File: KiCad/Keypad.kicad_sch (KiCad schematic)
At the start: 21 parts, among them J1 SPOX, J2 Molex, J3 USB-C, U1 ESP32-WROOM-32, U2 SP3458, U3 FT231XQ, U4 LMR16006YQ3

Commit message: Kicad tidy
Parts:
- C2: Note X7R or X5R 0603 -> (none)
- C3: Note 0603 or 0805 -> 0805
- C4: Note 0603 or 0805 -> 1206
- U1: footprint RevK:ESP32-WROOM-32 -> RF_Module:ESP32-WROOM-32
- U2: footprint Package_SO:SO-8_3.9x4.9mm_P1.27mm -> Package_SO:SO-8_5.3x6.2mm_P1.27mm
- U3: footprint RevK:QFN-20-1EP_4x4mm_P0.5mm_EP2.5x2.5mm -> Package_DFN_QFN:QFN-20-1EP_4x4mm_P0.5mm_EP2.5x2.5mm
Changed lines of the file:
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@@
   (title_block
     (title "Galaxy Keypad controller")
-    (date "2021-07-20")
+    (date "${DATE}")
     (rev "5")
     (company "Adrian Kennard Andrews & Arnold Ltd")
@@
     (property "Reference" "U2" (id 0) (at 106.68 152.019 0))
     (property "Value" "SP3458" (id 1) (at 106.68 154.3304 0))
-    (property "Footprint" "Package_SO:SO-8_3.9x4.9mm_P1.27mm" (id 2) (at 106.045 176.53 0)
+    (property "Footprint" "Package_SO:SO-8_5.3x6.2mm_P1.27mm" (id 2) (at 106.045 176.53 0)
       (effects (font (size 1.27 1.27)) hide)
     )
@@
     (property "Reference" "U3" (id 0) (at 172.085 88.7476 0))
     (property "Value" "FT231XQ" (id 1) (at 172.085 91.059 0))
-    (property "Footprint" "RevK:QFN-20-1EP_4x4mm_P0.5mm_EP2.5x2.5mm" (id 2) (at 206.375 136.525 0)
+    (property "Footprint" "Package_DFN_QFN:QFN-20-1EP_4x4mm_P0.5mm_EP2.5x2.5mm" (id 2) (at 206.375 136.525 0)
       (effects (font (size 1.27 1.27)) hide)
     )
@@
     (property "Reference" "U1" (id 0) (at 69.215 32.2326 0))
     (property "Value" "ESP32-WROOM-32" (id 1) (at 69.215 34.544 0))
-    (property "Footprint" "RevK:ESP32-WROOM-32" (id 2) (at 69.215 110.49 0)
+    (property "Footprint" "RF_Module:ESP32-WROOM-32" (id 2) (at 69.215 110.49 0)
       (effects (font (size 1.27 1.27)) hide)
     )
@@
     (pin "4")
   )
-  (symbol (lib_id "RevK:Hidden") (at 249.555 42.545 0) (unit 1)
-    (in_bom yes) (on_board yes)
-    (property "Reference" "C2" (id 0) (at 248.92 42.545 0)
+  (symbol (lib_name "Hidden_1") (lib_id "RevK:Hidden") (at 249.555 42.545 0) (unit 1)
+    (in_bom yes) (on_board yes)
+    (property "Reference" "C2" (id 0) (at 250.19 42.545 0)
       (effects (font (size 1.27 1.27)) (justify left))
     )
@@
       (effects (font (size 1.27 1.27)) hide)
     )
-    (property "Note" "X7R or X5R 0603" (id 4) (at 249.555 42.545 0)
+    (property "Note" "" (id 4) (at 249.555 42.545 0)
+      (effects (font (size 1.27 1.27)) hide)
+    )
+    (property "Part No" "" (id 5) (at 249.555 42.545 0)
       (effects (font (size 1.27 1.27)) hide)
     )
     (pin "~")
   )
-  (symbol (lib_id "RevK:Hidden") (at 249.555 44.45 0) (unit 1)
-    (in_bom yes) (on_board yes)
-    (property "Reference" "C3" (id 0) (at 248.92 44.45 0)
+  (symbol (lib_name "Hidden_2") (lib_id "RevK:Hidden") (at 249.555 44.45 0) (unit 1)
+    (in_bom yes) (on_board yes)
+    (property "Reference" "C3" (id 0) (at 250.19 44.45 0)
       (effects (font (size 1.27 1.27)) (justify left))
     )
@@
       (effects (font (size 1.27 1.27)) hide)
     )
-    (property "Note" "0603 or 0805" (id 4) (at 249.555 44.45 0)
+    (property "Note" "0805" (id 4) (at 249.555 44.45 0)
+      (effects (font (size 1.27 1.27)) hide)
+    )
+    (property "Part No" "" (id 5) (at 249.555 44.45 0)
       (effects (font (size 1.27 1.27)) hide)
     )
     (pin "~")
   )
-  (symbol (lib_id "RevK:Hidden") (at 249.555 46.355 0) (unit 1)
-    (in_bom yes) (on_board yes)
-    (property "Reference" "C4" (id 0) (at 248.92 46.355 0)
+  (symbol (lib_name "Hidden_3") (lib_id "RevK:Hidden") (at 249.555 46.355 0) (unit 1)
+    (in_bom yes) (on_board yes)
+    (property "Reference" "C4" (id 0) (at 250.19 46.355 0)
       (effects (font (size 1.27 1.27)) (justify left))
     )
@@
       (effects (font (size 1.27 1.27)) hide)
     )
-    (property "Note" "0603 or 0805" (id 4) (at 249.555 46.355 0)
+    (property "Note" "1206" (id 4) (at 249.555 46.355 0)
+      (effects (font (size 1.27 1.27)) hide)
+    )
+    (property "Part No" "" (id 5) (at 249.555 46.355 0)
       (effects (font (size 1.27 1.27)) hide)
     )
     (pin "~")
   )
-  (symbol (lib_id "RevK:Hidden") (at 249.555 48.26 0) (unit 1)
-    (in_bom yes) (on_board yes)
-    (property "Reference" "L1" (id 0) (at 248.92 48.26 0)
+  (symbol (lib_name "Hidden_4") (lib_id "RevK:Hidden") (at 249.555 48.26 0) (unit 1)
+    (in_bom yes) (on_board yes)
+    (property "Reference" "L1" (id 0) (at 250.19 48.26 0)
       (effects (font (size 1.27 1.27)) (justify left))
     )
@@
       (effects (font (size 1.27 1.27)) hide)
     )
+    (property "Note" "" (id 6) (at 256.54 58.42 0))
     (pin "~")
   )
   (symbol (lib_id "RevK:Hidden") (at 249.555 50.165 0) (unit 1)
     (in_bom yes) (on_board yes)
-    (property "Reference" "D3" (id 0) (at 248.92 50.165 0)
+    (property "Reference" "D3" (id 0) (at 250.19 50.165 0)
       (effects (font (size 1.27 1.27)) (justify left))
     )
@@
       (effects (font (size 1.27 1.27)) hide)
     )
+    (property "Note" "" (id 6) (at 256.54 55.88 0))
     (pin "~")
   )
@@
     )
     (path "/00000000-0000-0000-0000-000060cc7ad0"
-      (reference "U1") (unit 1) (value "ESP32-WROOM-32") (footprint "RevK:ESP32-WROOM-32")
+      (reference "U1") (unit 1) (value "ESP32-WROOM-32") (footprint "RF_Module:ESP32-WROOM-32")
     )
     (path "/00000000-0000-0000-0000-000060718926"
-      (reference "U2") (unit 1) (value "SP3458") (footprint "Package_SO:SO-8_3.9x4.9mm_P1.27mm")
+      (reference "U2") (unit 1) (value "SP3458") (footprint "Package_SO:SO-8_5.3x6.2mm_P1.27mm")
     )
     (path "/00000000-0000-0000-0000-00006084108b"
-      (reference "U3") (unit 1) (value "FT231XQ") (footprint "RevK:QFN-20-1EP_4x4mm_P0.5mm_EP2.5x2.5mm")
+      (reference "U3") (unit 1) (value "FT231XQ") (footprint "Package_DFN_QFN:QFN-20-1EP_4x4mm_P0.5mm_EP2.5x2.5mm")
     )
     (path "/00000000-0000-0000-0000-0000610ee400"

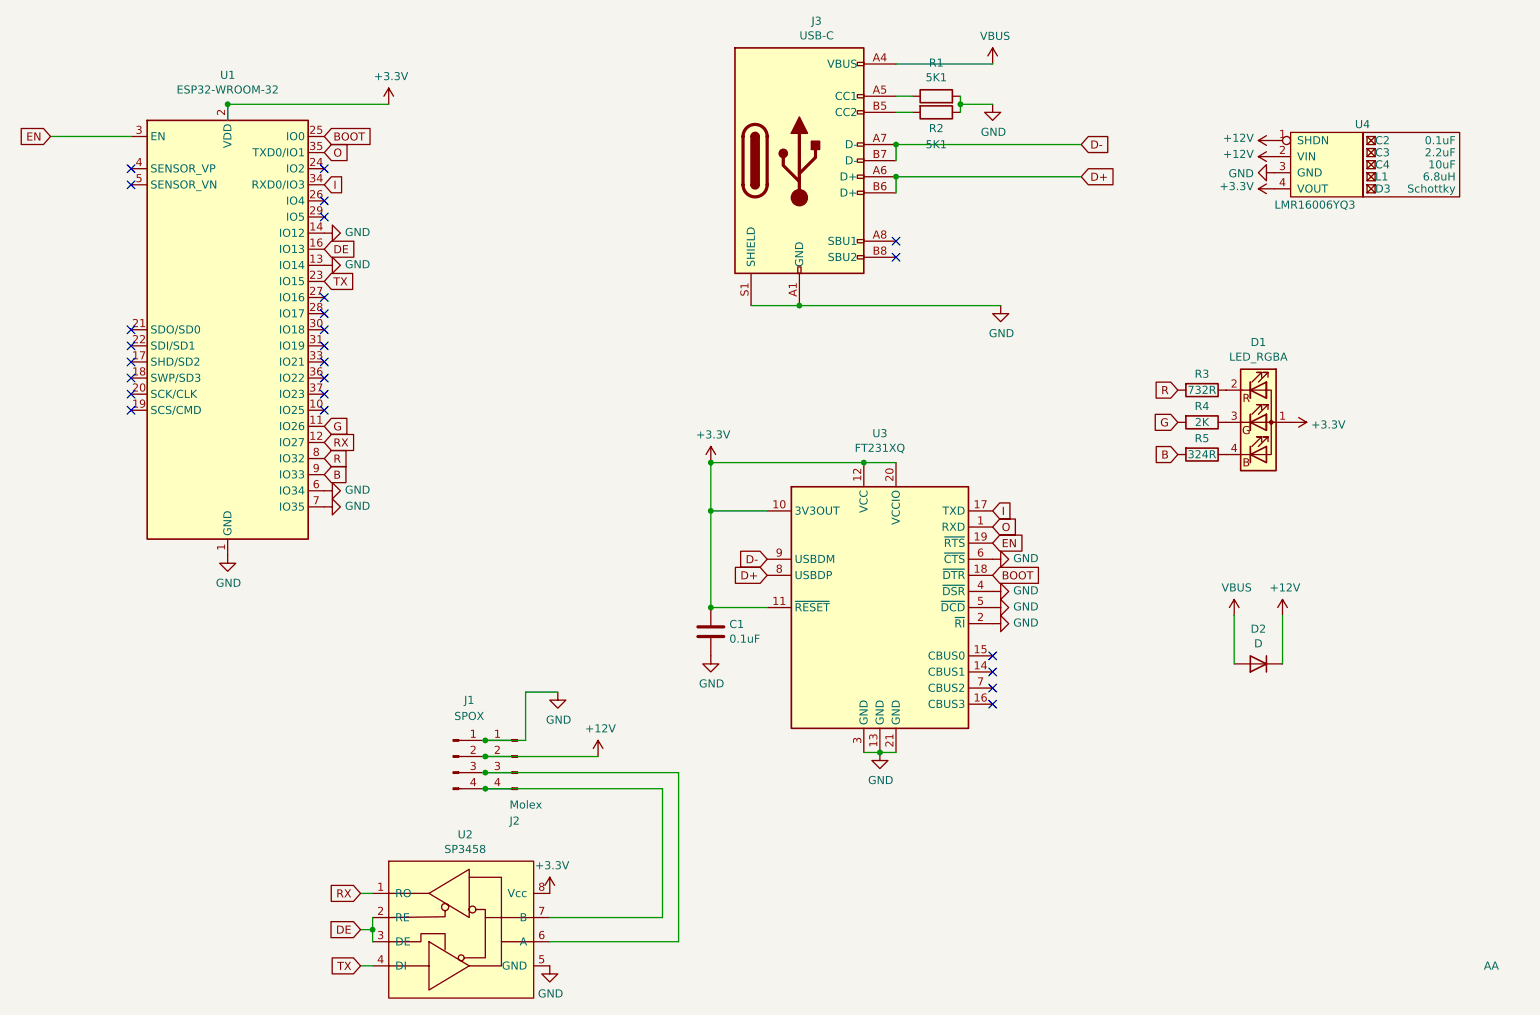
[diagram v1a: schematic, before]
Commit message: Rework for PSu change
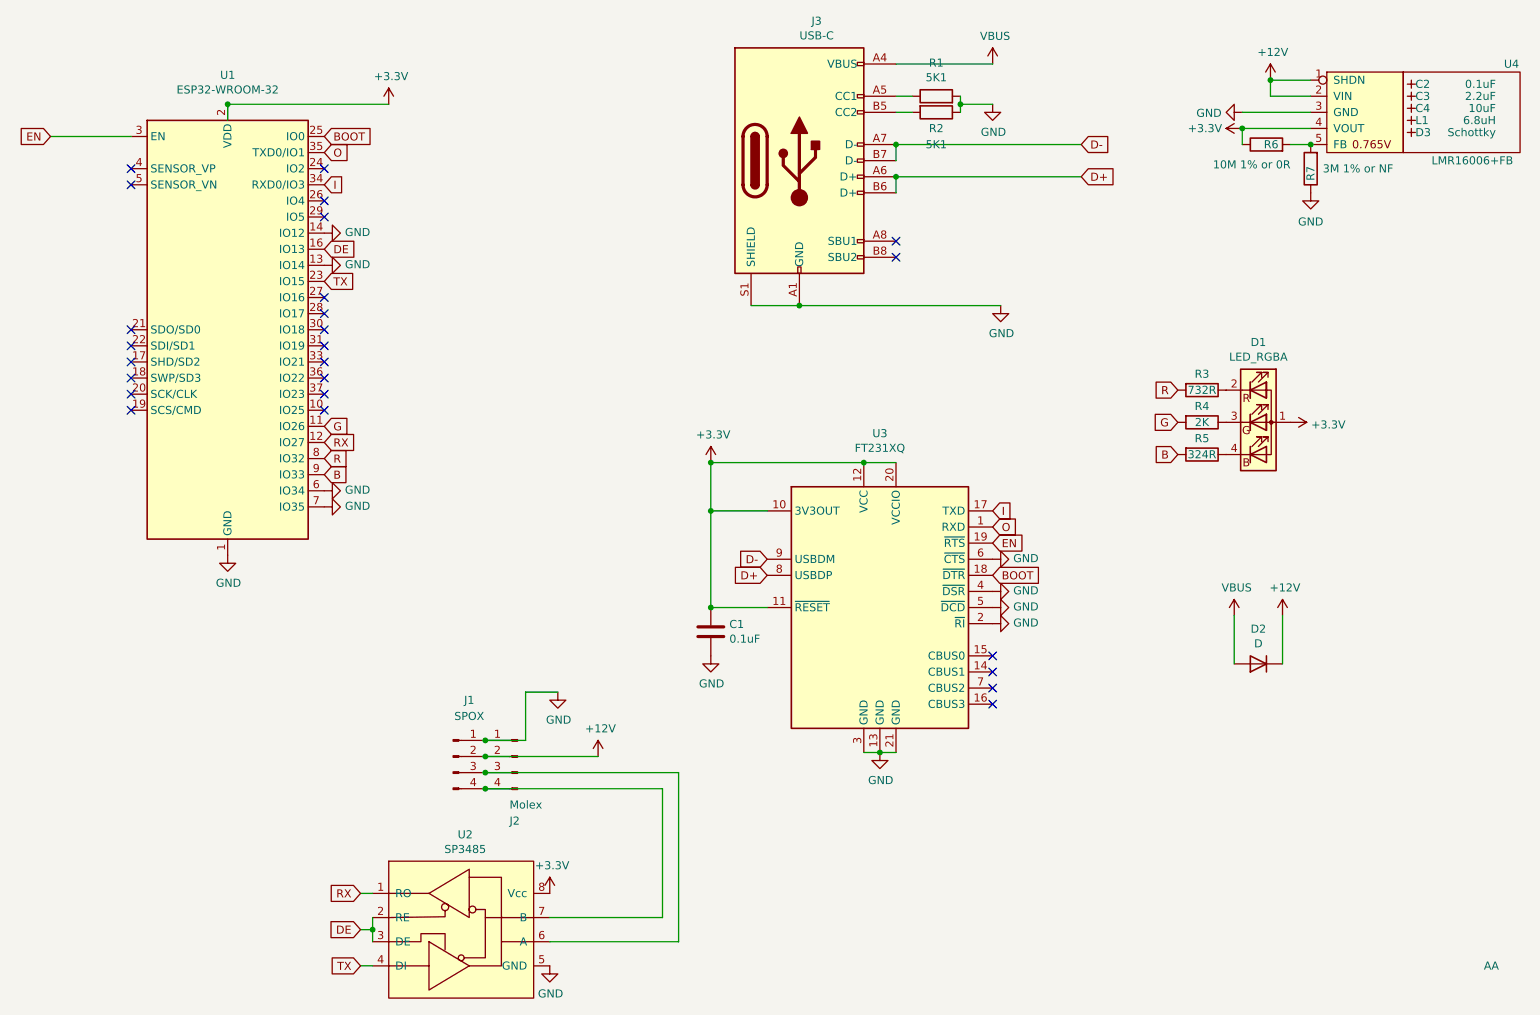
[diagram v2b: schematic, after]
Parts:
- removed U4: LMR16006YQ3, RevK:RegulatorBlock, symbol RevK:LMR16006YQ3
- added R6: 10M 1% or 0R, RevK:R_0603, symbol Device:R
- added R7: 3M 1% or NF, RevK:R_0603, symbol Device:R
- added U4: LMR16006+FB, RevK:RegulatorBlockFB, symbol RevK:LMR16006+FB
- Logo1: Note (none) -> Non part, PCB printed
- U1: footprint RF_Module:ESP32-WROOM-32 -> RevK:ESP32-WROOM-32
- U2: value SP3458 -> SP3485; footprint Package_SO:SO-8_5.3x6.2mm_P1.27mm -> Package_SO:SOIC-8_3.9x4.9mm_P1.27mm
- U3: footprint Package_DFN_QFN:QFN-20-1EP_4x4mm_P0.5mm_EP2.5x2.5mm -> RevK:QFN-20-1EP_4x4mm_P0.5mm_EP2.5x2.5mm
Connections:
- net +12V: now also U4.1 (SHDN), U4.2 (VIN)
- net +3V3: now also R6.1, U4.4 (VOUT)
- net GND: now also R7.1, U4.3 (GND)
- new net: R6.2, R7.2, U4.5 (FB)

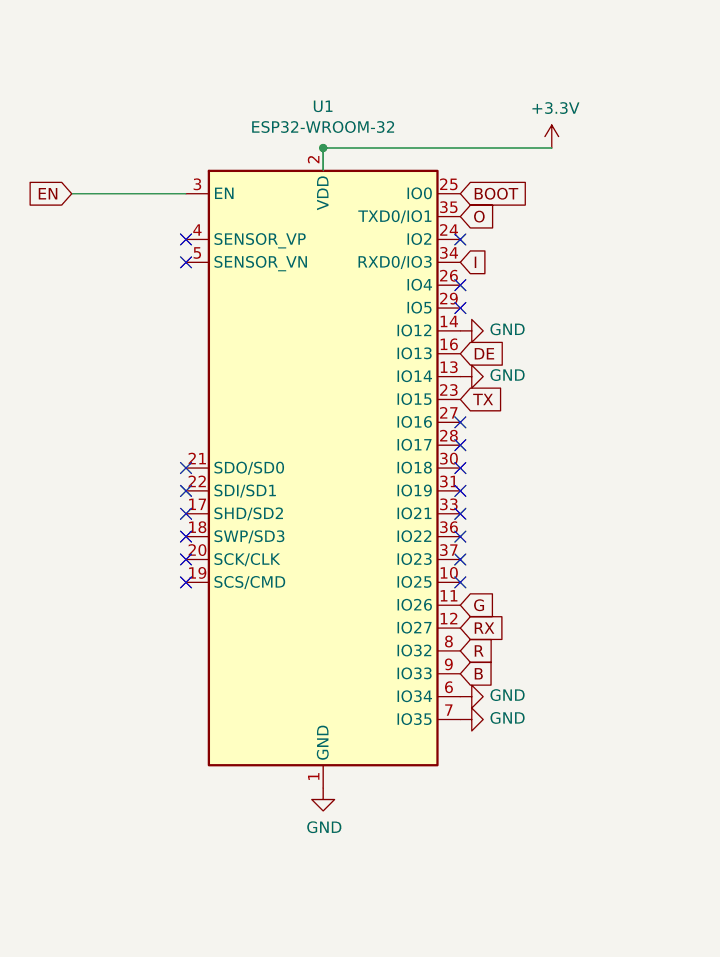
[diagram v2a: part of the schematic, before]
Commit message: Updated for VBUS and GPIO changes
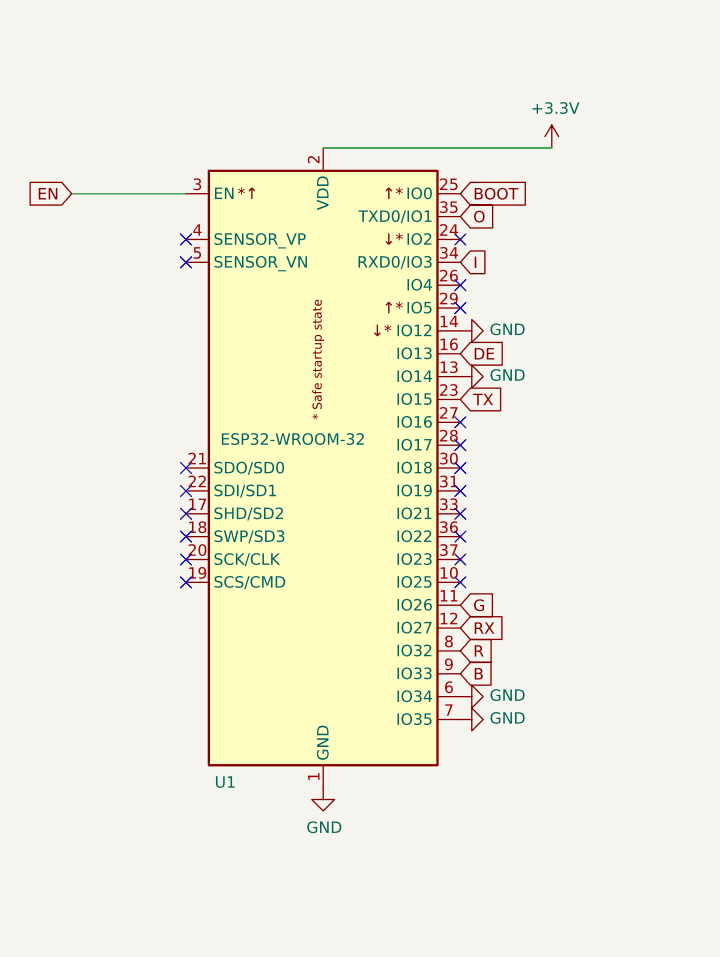
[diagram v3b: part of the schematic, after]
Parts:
- removed U1: ESP32-WROOM-32, RevK:ESP32-WROOM-32, symbol RF_Module:ESP32-WROOM-32
- added U1: ESP32-WROOM-32, RevK:ESP32-WROOM-32, symbol RevK:ESP32-WROOM-32
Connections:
- net +3V3: now also U1.2 (VDD)
- net B: now also U1.9 (IO33)
- net BOOT: now also U1.25 (IO0)
- net DE: now also U1.16 (IO13)
- net EN: now also U1.3 (EN)
- net G: now also U1.11 (IO26)
- net GND: now also U1.1 (GND), U1.13 (IO14), U1.14 (IO12), U1.15 (GND), U1.38 (GND), U1.39 (GND), U1.6 (IO34), U1.7 (IO35)
- net I: now also U1.34 (RXD0/IO3)
- net O: now also U1.35 (TXD0/IO1)
- net R: now also U1.8 (IO32)
- net RX: now also U1.12 (IO27)
- net TX: now also U1.23 (IO15)
